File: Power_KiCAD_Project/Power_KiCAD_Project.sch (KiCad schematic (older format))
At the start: 6 parts, among them J1 XT60-M, J2 XT60-M, J3 XT60-M, J4 XT60-M, J5 XT60-M, J6 PJ-102AH

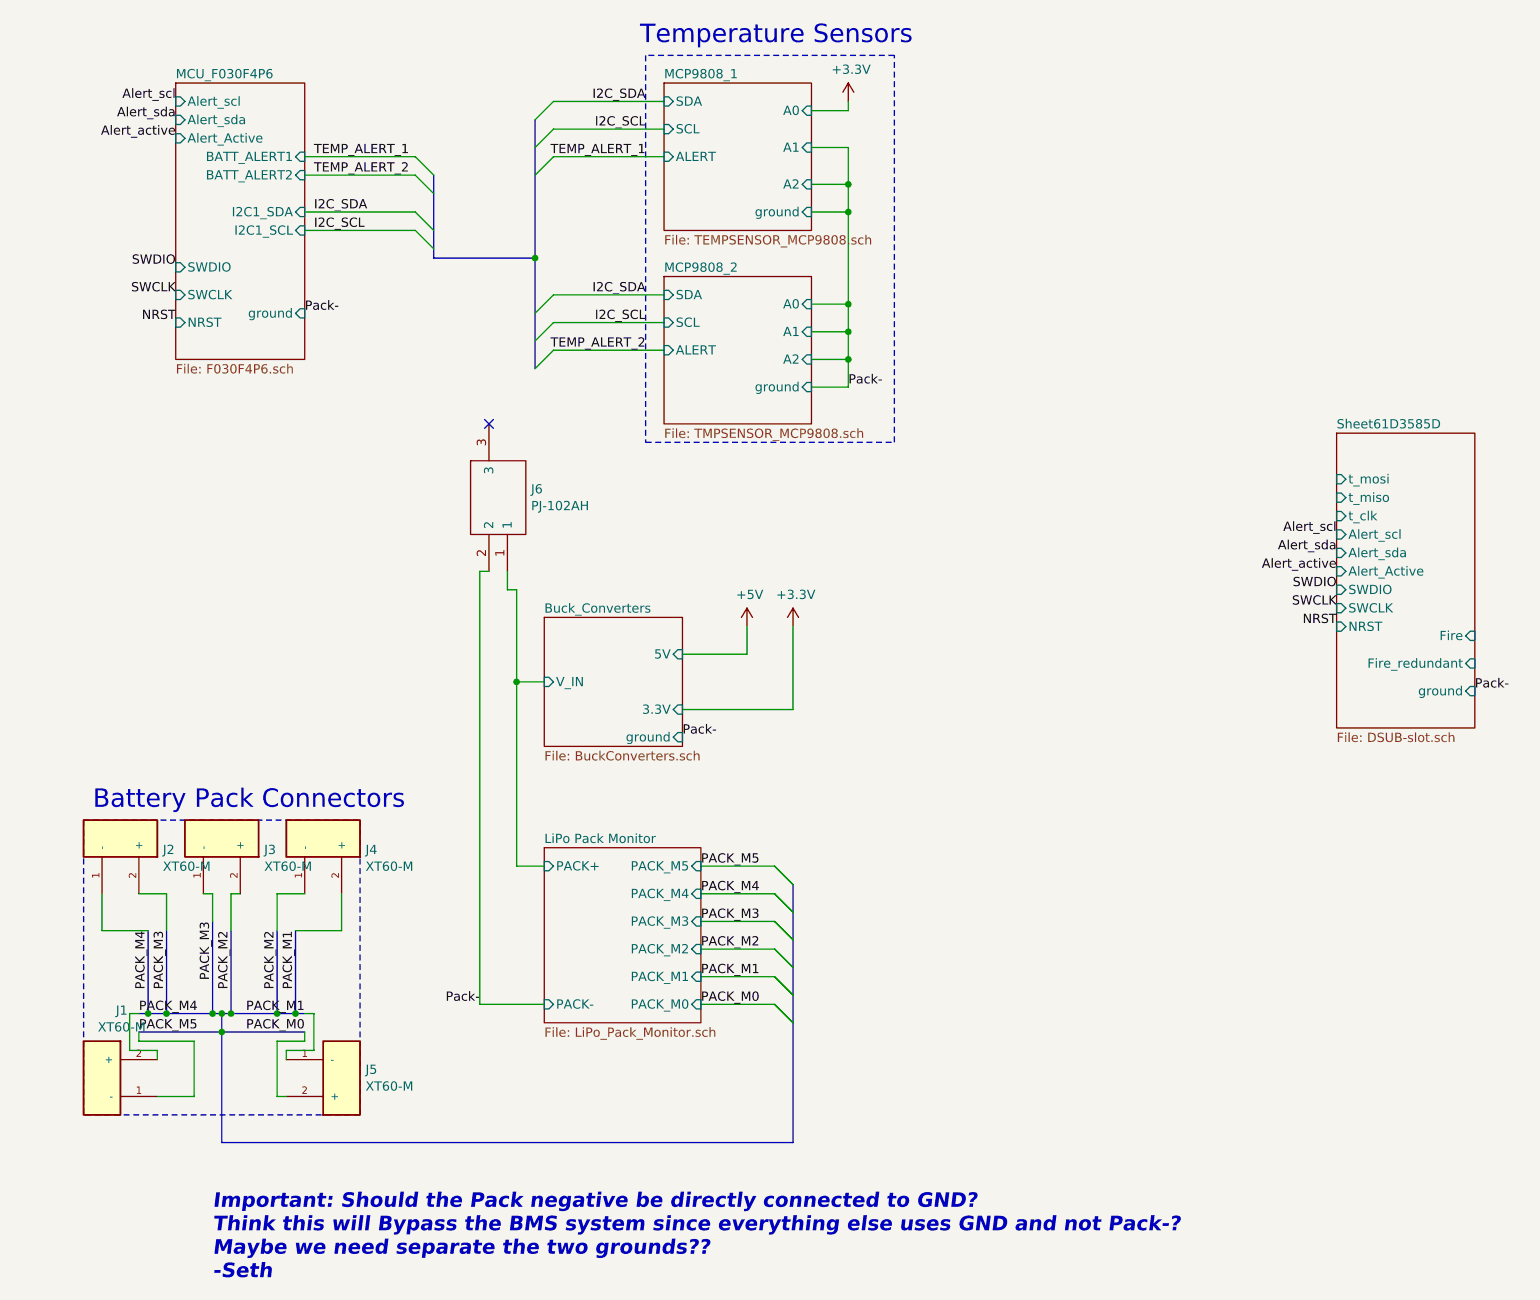
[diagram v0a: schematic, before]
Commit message: Changes to PCB
re did the pcb and added a "switch"
basically its just an xt60 connector in series with the other ones that needs to be shorted for the board to get power
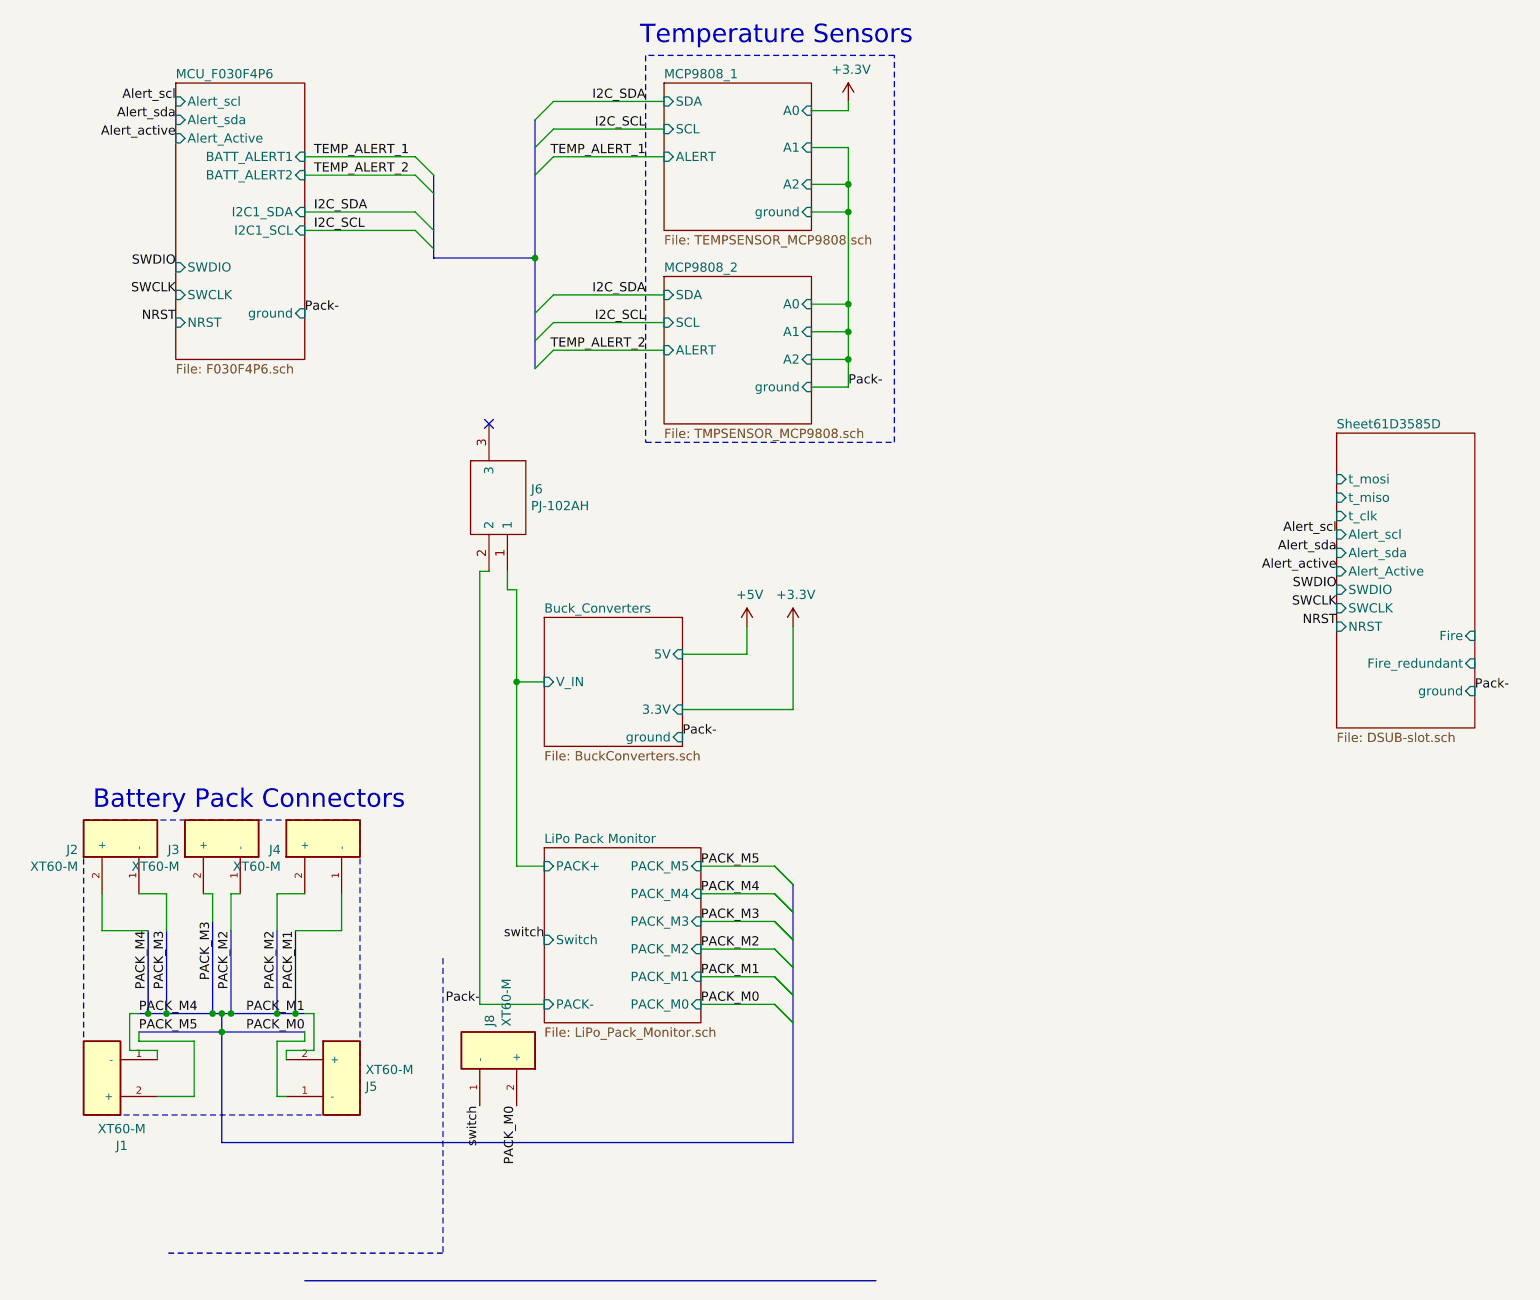
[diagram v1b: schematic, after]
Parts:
- added J8: XT60-M, XT60-M:AMASS_XT60-M, symbol XT60-M:XT60-M
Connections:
- net PACK_M0: now also J5.1 (-), J8.2 (+); no longer J5.2 (+)
- net PACK_M1: now also J4.1 (-), J5.2 (+); no longer J4.2 (+), J5.1 (-)
- net PACK_M2: now also J3.1 (-), J4.2 (+); no longer J3.2 (+), J4.1 (-)
- net PACK_M3: now also J2.1 (-), J3.2 (+); no longer J2.2 (+), J3.1 (-)
- net PACK_M4: now also J1.1 (-), J2.2 (+); no longer J1.2 (+), J2.1 (-)
- net PACK_M5: now also J1.2 (+); no longer J1.1 (-)
- new net switch: J8.1 (-)
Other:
- note removed: "Important: Should the Pack negative be directly connected to GND?\nThink this will Bypass the BMS system since everything else uses GND and not Pack-?\nMaybe we need separate the two grounds??\n-Seth"
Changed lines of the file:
@@
 Wire Wire Line
 	4450 4450 3850 4450
-Text Notes 1300 7550 0    79   Italic 16
-Important: Should the Pack negative be directly connected to GND?\nThink this will Bypass the BMS system since everything else uses GND and not Pack-?\nMaybe we need separate the two grounds??\n-Seth
 Wire Wire Line
 	4550 1750 4750 1750
@@
 F 9 "Plug; DC supply; XT60; male; PIN: 2; for cable; soldered; 30A; 500V" H 800 5150 50  0001 L BNN "Description"
 	1    800  5150
-	0    -1   -1   0
+	0    1    -1   0
 $EndComp
 $Comp
@@
 F 9 "Plug; DC supply; XT60; male; PIN: 2; for cable; soldered; 30A; 500V" H 1350 5150 50  0001 L BNN "Description"
 	1    1350 5150
-	0    -1   -1   0
+	0    1    -1   0
 $EndComp
 $Comp
@@
 F 9 "Plug; DC supply; XT60; male; PIN: 2; for cable; soldered; 30A; 500V" H 1900 5150 50  0001 L BNN "Description"
 	1    1900 5150
-	0    -1   -1   0
+	0    1    -1   0
 $EndComp
 $Comp
@@
 F 9 "Plug; DC supply; XT60; male; PIN: 2; for cable; soldered; 30A; 500V" H 700 6450 50  0001 L BNN "Description"
 	1    700  6450
-	-1   0    0    1
+	-1   0    0    -1
 $EndComp
 $Comp
@@
 F 9 "Plug; DC supply; XT60; male; PIN: 2; for cable; soldered; 30A; 500V" H 2000 6450 50  0001 L BNN "Description"
 	1    2000 6450
-	1    0    0    -1
+	1    0    0    1
 $EndComp
 Wire Wire Line
@@
 F8 "PACK_M0" I R 3950 6050 50
 F9 "PACK-" I L 3100 6050 50
+F10 "Switch" I L 3100 5700 50
 $EndSheet
 Wire Bus Line
+	1800 7550 4900 7550
+Wire Notes Line
+	2550 5800 2550 7400
+Wire Notes Line
+	2550 7400 1050 7400
+$Comp
+L XT60-M:XT60-M J8
+U 1 1 61C843A7
+P 2850 6300
+F 0 "J8" H 2980 6346 50  0000 L CNN
+F 1 "XT60-M" H 2980 6255 50  0000 L CNN
+F 2 "XT60-M:AMASS_XT60-M" H 2850 6300 50  0001 L BNN
+F 3 "" H 2850 6300 50  0001 L BNN
+F 4 "XT60-M" H 2850 6300 50  0001 L BNN "MP"
+F 5 "None" H 2850 6300 50  0001 L BNN "Price"
+F 6 "Package" H 2850 6300 50  0001 L BNN "Package"
+F 7 "AMASS" H 2850 6300 50  0001 L BNN "MF"
+F 8 "Not in stock" H 2850 6300 50  0001 L BNN "Availability"
+F 9 "Plug; DC supply; XT60; male; PIN: 2; for cable; soldered; 30A; 500V" H 2850 6300 50  0001 L BNN "Description"
+	1    2850 6300
+	0    -1   -1   0
+$EndComp
+Wire Bus Line
 	3050 2000 3050 2600
 Wire Bus Line
@@
 Wire Bus Line
 	4450 5400 4450 6800
+Text Label 2950 6600 3    50   ~ 0
+PACK_M0
+Text Label 2750 6600 3    50   ~ 0
+switch
+Text Label 3100 5700 2    50   ~ 0
+switch
 $EndSCHEMATC
